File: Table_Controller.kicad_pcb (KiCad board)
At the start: 4 copper layers, 80 x 49.1 mm, 103 parts, among them J1 Dell DC jack, J11 HX JN1.27-2x5 WZ H4.9, J12 JST B4B XH A, J13 Conn_01x14_Pin, J14 JST B6B XH A, J15 2.54 mm header, J2 USB_C_Receptacle_USB2.0_16P, U10 STM32G431K8Tx, U11 LMR380x0, U12 VNH7070, Y10 20 MHz

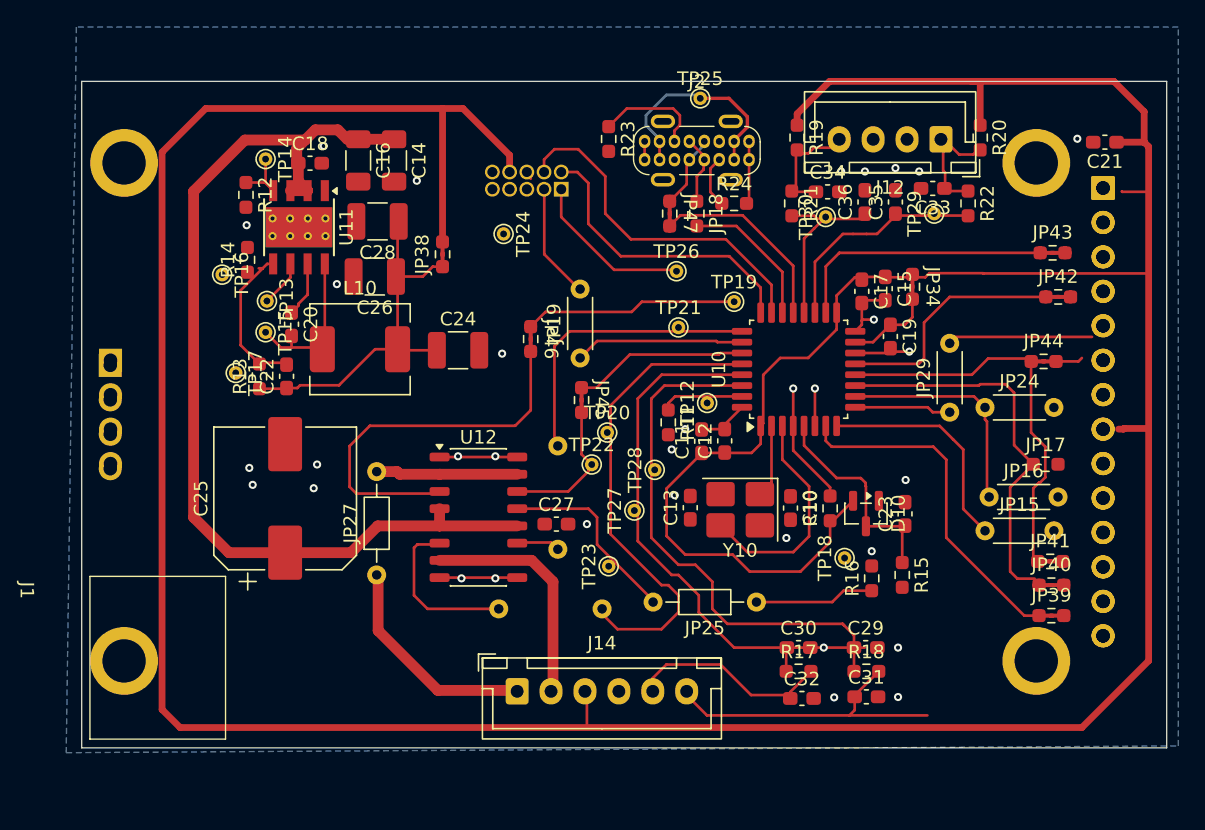
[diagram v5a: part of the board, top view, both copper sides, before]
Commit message: concept placement finalised
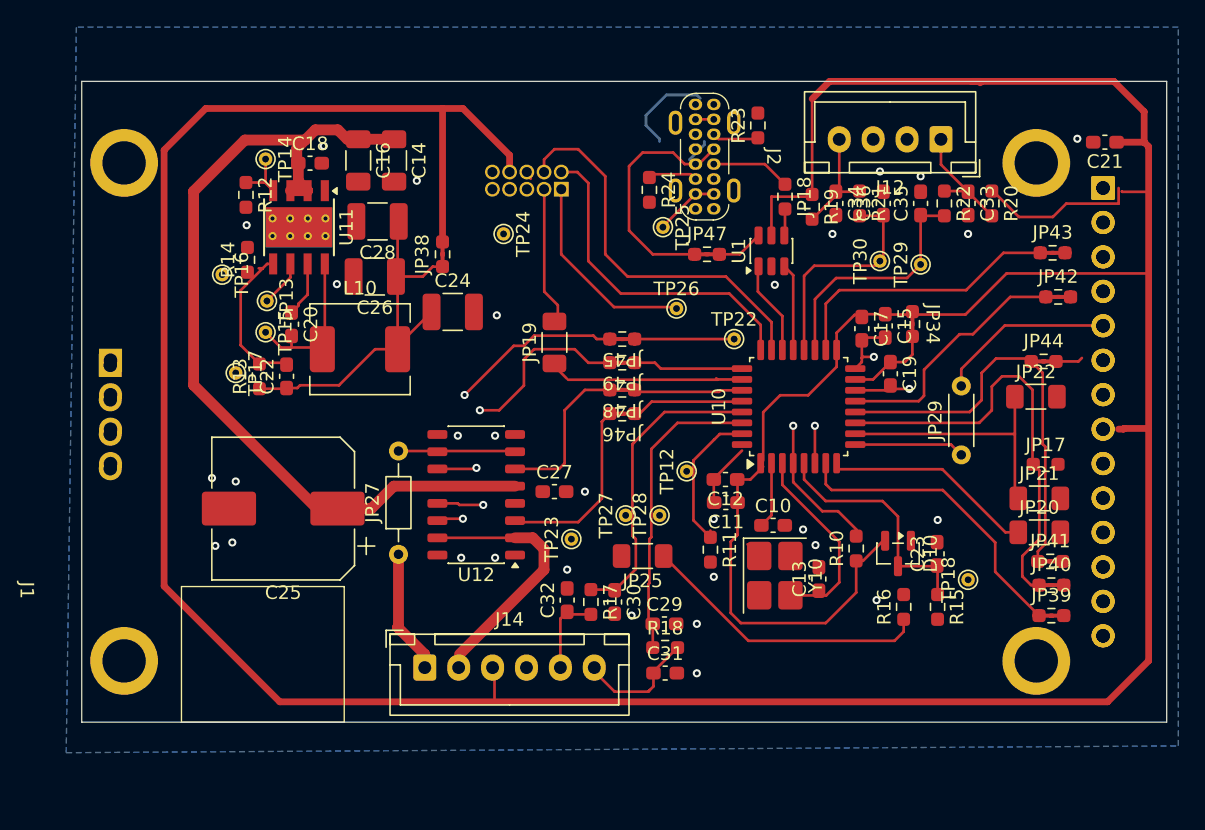
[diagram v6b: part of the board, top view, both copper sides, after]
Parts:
- removed JP15, JP16, JP24: 0R, Resistor_THT:R_Axial_DIN0204_L3.6mm_D1.6mm_P5.08mm_Horizontal
- removed JP26, JP32: 0R, Resistor_THT:R_Axial_DIN0204_L3.6mm_D1.6mm_P7.62mm_Horizontal
- removed TP19, TP20, TP21: TestPoint, TestPoint:TestPoint_THTPad_D1.0mm_Drill0.5mm
- added JP20: 0R, Resistor_SMD:R_1206_3216Metric_Pad1.30x1.75mm_HandSolder, F.Cu at (152.8, 119.2)
- added JP21: 0R, Resistor_SMD:R_1206_3216Metric_Pad1.30x1.75mm_HandSolder, F.Cu at (152.8, 116.8)
- added JP22: 0R, Resistor_SMD:R_1206_3216Metric_Pad1.30x1.75mm_HandSolder, F.Cu at (152.5, 109.2)
- added JP48: 0R, Personal:Jumper_0603, F.Cu at (122.0, 108.8)
- added JP49: 0R, Personal:Jumper_0603, F.Cu at (122.0, 106.7)
- added U1: USBLC6-2SC6, Package_TO_SOT_SMD:SOT-23-6, F.Cu at (133.0, 98.5)
- JP19: footprint Resistor_THT:R_Axial_DIN0204_L3.6mm_D1.6mm_P5.08mm_Horizontal -> Resistor_SMD:R_1206_3216Metric_Pad1.30x1.75mm_HandSolder
- JP25: footprint Resistor_THT:R_Axial_DIN0204_L3.6mm_D1.6mm_P7.62mm_Horizontal -> Resistor_SMD:R_1206_3216Metric_Pad1.30x1.75mm_HandSolder
- moved C32 18.8 mm to (117.9, 124.2), turned to 90 degrees
- moved R17 16.1 mm to (119.7, 124.4), turned to -90 degrees
- moved C29 14.9 mm to (125.1, 126.0)
- moved C31 14.9 mm to (125.2, 129.6)
- moved R18 14.9 mm to (125.2, 127.8)
- moved TP22 14.0 mm to (130.2, 105.0)
- moved C30 14.0 mm to (121.4, 124.4), turned to -90 degrees
- moved R23 11.0 mm to (132.0, 89.2), turned to 90 degrees
- moved C13 10.8 mm to (136.5, 122.7)
- moved TP25 9.89 mm to (125.0, 96.8), turned to -90 degrees
- moved R11 9.89 mm to (128.5, 120.5)
- moved TP18 9.25 mm to (147.5, 122.8)
- moved JP25 9.05 mm to (123.5, 121.0)
- moved JP46 8.71 mm to (122.0, 110.5), turned to 180 degrees
- moved J14 7.03 mm to (107.4, 129.2)
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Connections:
- J14 pad 1: /OUTa -> /OUTb
- J14 pad 2: /OUTb -> /OUTa
- JP18 pad 1: Net-(J2-D+-PadA6) -> Net-(J2-D--PadA7)
- JP18 pad 2: /USB_DP -> Net-(JP18-Pad2)
- JP27 pad 1: /OUTa -> /OUTb
- JP27 pad 2: /OUTa' -> Net-(JP27-Pad2)
- JP47 pad 1: Net-(J2-D--PadA7) -> Net-(J2-D+-PadA6)
- JP47 pad 2: /USB_DM -> Net-(JP47-Pad2)
- TP22 pad 1: /SEL0' -> /SEL0
- U10 pad 27: /SEL0 -> /INb
- U10 pad 28: /INb -> /INa
- U10 pad 6: /INa -> /SEL0
- U12 pad 10: /OUTb -> Net-(JP27-Pad2)
- U12 pad 15: /OUTa' -> /OUTa
- U12 pad 2: /OUTa' -> /OUTa
- U12 pad 7: /OUTb -> Net-(JP27-Pad2)
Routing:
- net /INb: track 35.6 -> 8.03 mm
- net /INa: track 27.7 -> 8.30 mm, vias 1 -> 0
- net /ENCa_filt: track 41.4 -> 22.6 mm
- net /PWM': track 3.22 -> 20.4 mm, vias 0 -> 2
- net /ENCb_filt: track 39.3 -> 22.3 mm
- net /GND: track 30.6 -> 14.4 mm, vias 31 -> 32
- net /INa': track 28.7 -> 13.7 mm
- net /PWM: track 21.7 -> 8.10 mm
- net /ENCb: track 23.2 -> 9.56 mm
- net /SEL0': track 10.6 -> 23.8 mm, vias 0 -> 2
- net Net-(JP25-Pad1): track 8.85 -> 21.5 mm
- net Net-(J2-D+-PadA6): track 5.10 -> 17.5 mm
- net /OUTa': track 10.4 -> 0.00 mm
- net /S3V3: track 306.0 -> 316.0 mm
- net /ENCa: track 15.2 -> 6.35 mm
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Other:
- board size 80 x 49.1 mm -> 80 x 47.2 mm

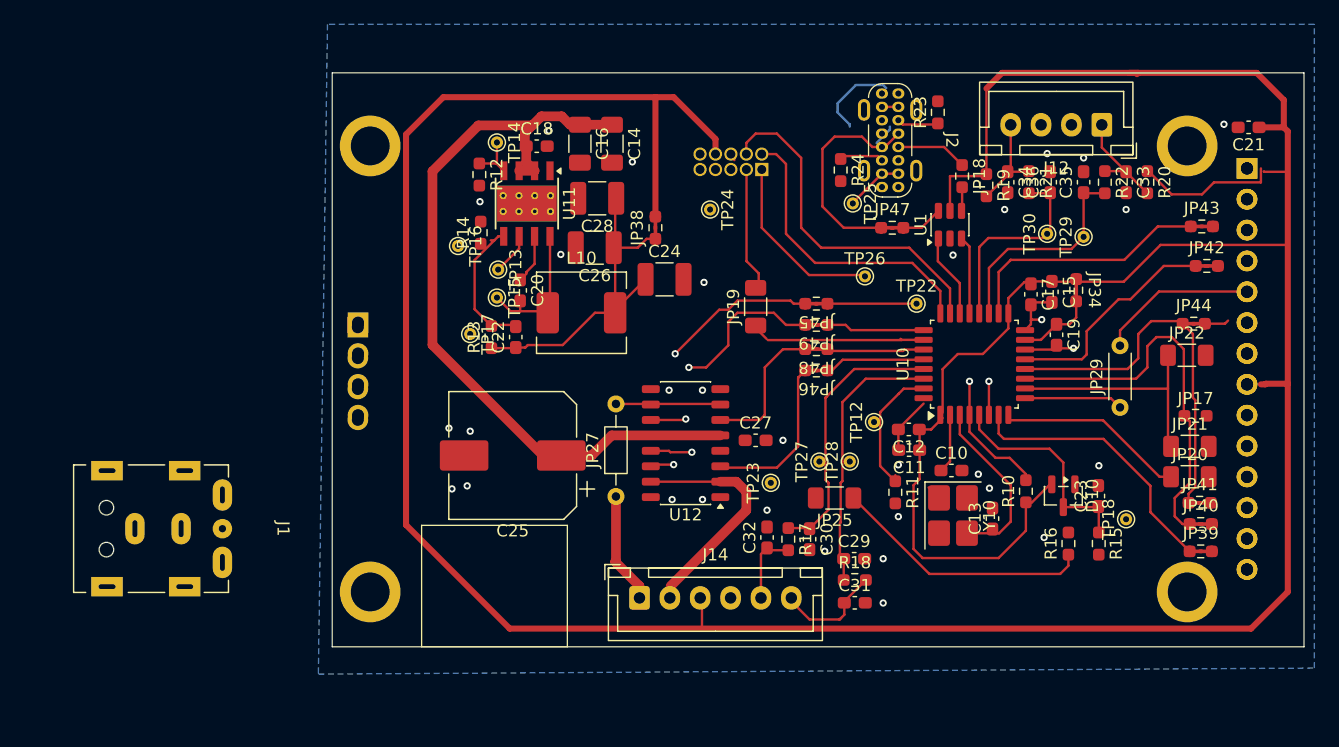
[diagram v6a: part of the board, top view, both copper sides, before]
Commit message: reworked DC barrel jack
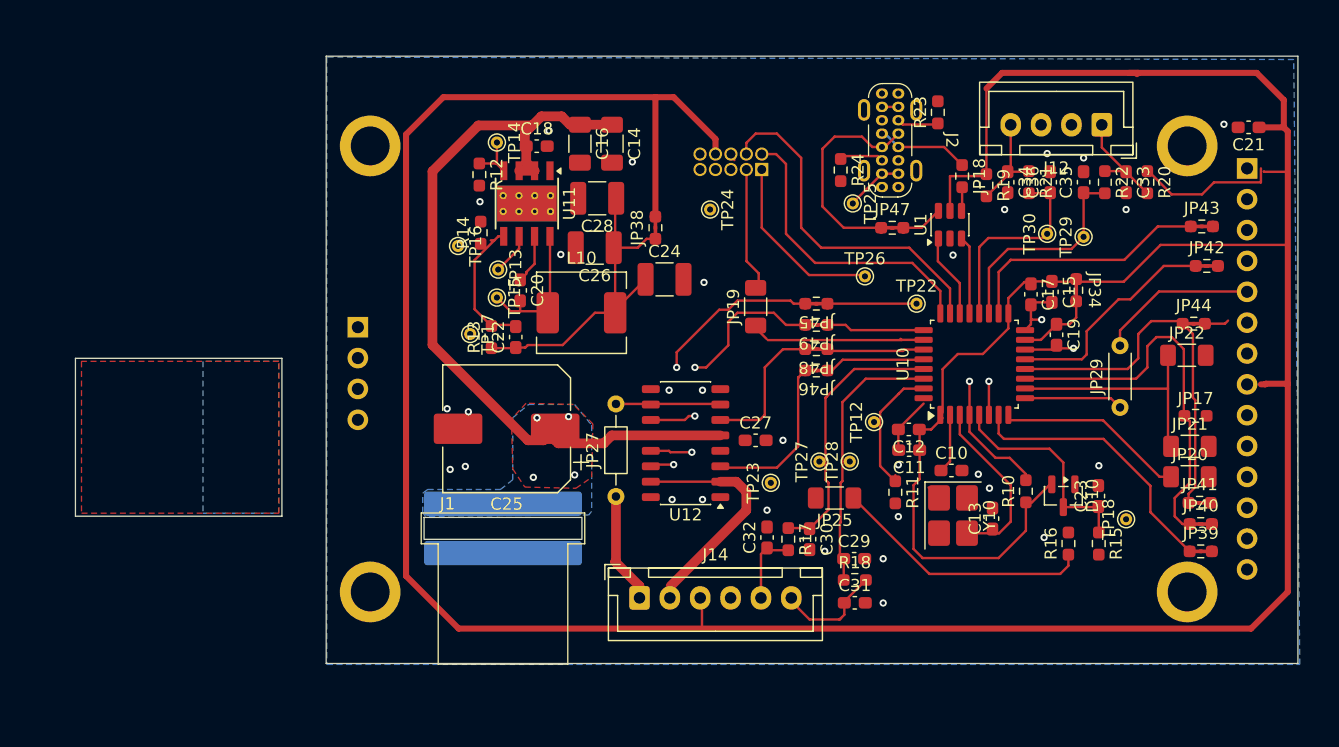
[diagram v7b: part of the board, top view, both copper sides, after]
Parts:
- J1: footprint Personal:Dell DC jack -> Personal:Dell_barrel_assy
- TFT10: footprint Personal:Display_240x320_ILI9341_2.4in -> Personal:Display_240x320_ILI9341_2.4in_no_pads
- moved J1 35.4 mm to (96.2, 123.5), turned to 0 degrees
- moved C25 2.26 mm to (96.5, 115.3)
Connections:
- J1 pad 1: /S19V5 -> /S19V5_2
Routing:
- net Net-(J2-VBUS-PadA4): track 12.9 -> 5.79 mm
- net /S3V3: track 316.0 -> 318.5 mm
- net /S19V5: track 65.0 -> 65.5 mm, vias 0 -> 4
- added copper zone on F.Cu, net /GND_2
- added copper zone on B.Cu, net /S19V5
- added copper zone on F.Cu, net /S19V5
- added copper zone on B.Cu, net /S19V5_2
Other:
- board size 80 x 47.2 mm -> 100.6 x 50 mm

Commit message: sch erc done, clear
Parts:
- added J3: DC barrel assy, Personal:Dell_barrel_assy, F.Cu at (96.6, 123.4)
- J1: footprint Personal:Dell_barrel_assy -> Personal:Dell DC jack
- moved J1 35.8 mm to (61.2, 115.9), turned to -90 degrees
- moved C25 0.20 mm to (96.5, 115.5)
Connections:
- net Net-(C22-Pad1) renamed /3V3_REG
- net Net-(J11-Pin_3) renamed /SWO'
- net Net-(J2-CC1) renamed /CC1
- net Net-(J2-CC2) renamed /CC2
- net Net-(J2-D+-PadA6) renamed /D+
- net Net-(J2-D--PadA7) renamed /D-
- net Net-(JP18-Pad2) renamed /D-'
- net Net-(JP27-Pad2) renamed /OUTb'
- net Net-(JP47-Pad2) renamed /D+'
- net Net-(U11-FB) renamed /FB
- net Net-(U11-PG) renamed /PG
- net Net-(U11-RT/SYNC) renamed /RT
- net Net-(U11-SW) renamed /SW
